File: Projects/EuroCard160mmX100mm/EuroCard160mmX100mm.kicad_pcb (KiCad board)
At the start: 2 copper layers, 159.8 x 99.8 mm, 0 parts

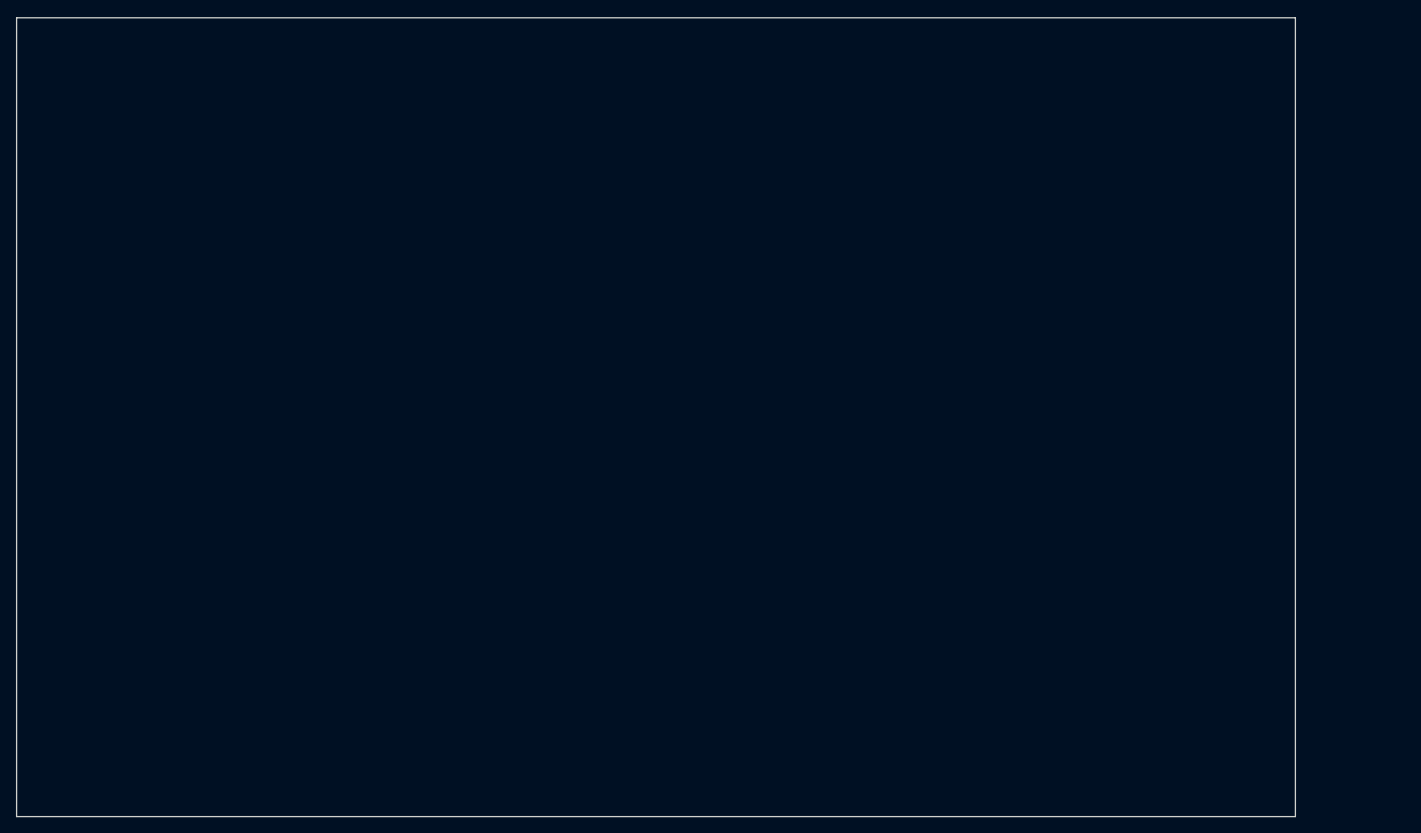
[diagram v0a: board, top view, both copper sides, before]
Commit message: Update EuroCard160mmX100mm* using KiCad 5.1.6
* Repointed all symbols and footprints to current libraries.
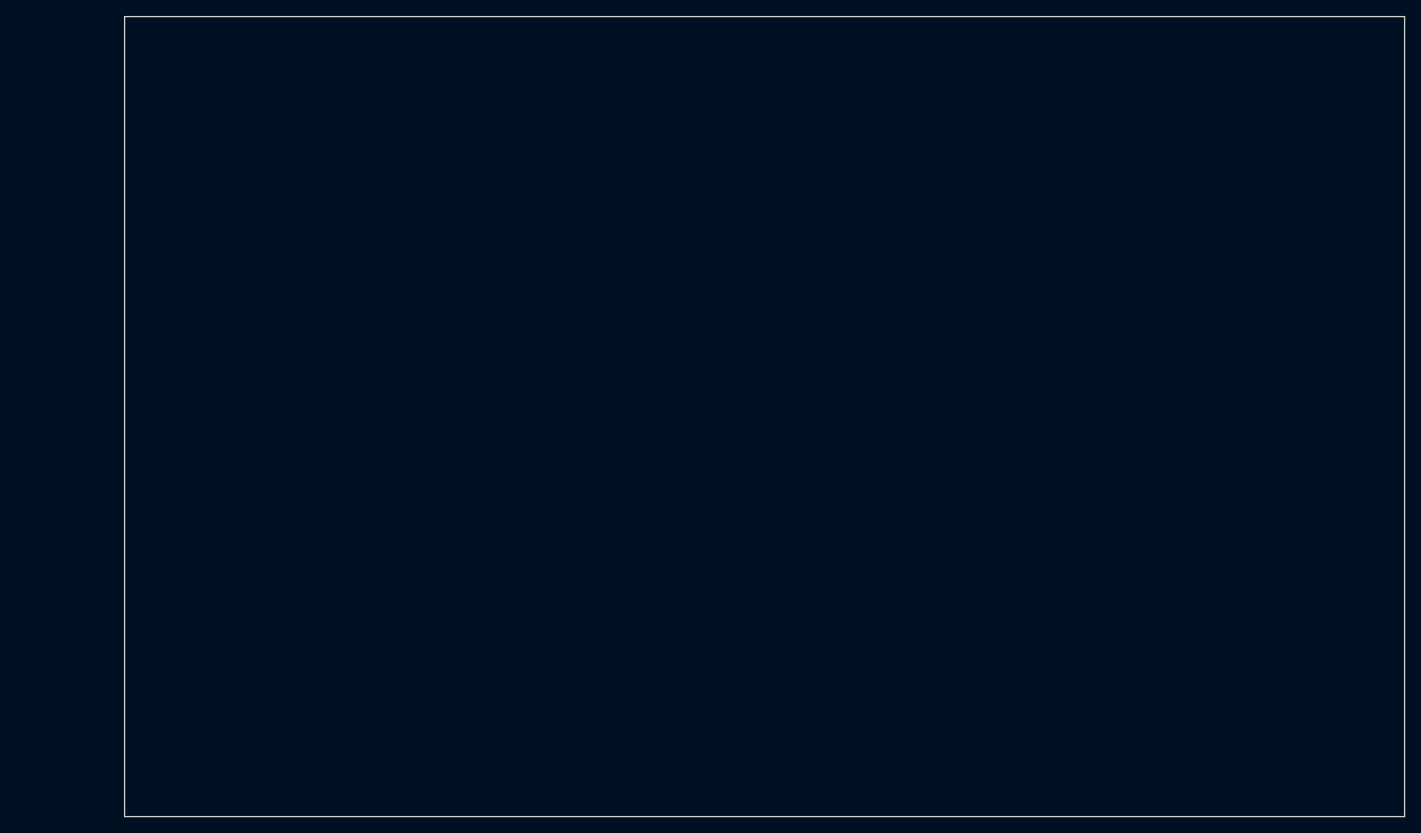
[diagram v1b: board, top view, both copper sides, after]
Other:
- board size 159.8 x 99.8 mm -> 160 x 100 mm
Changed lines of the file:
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@@
-(kicad_pcb (version 20170123) (host pcbnew "(2017-07-16 revision e797af331)-master")
+(kicad_pcb (version 20171130) (host pcbnew "(5.1.6)-1")
   (general
     (thickness 1.6)
@@
     (zone_45_only no)
     (trace_min 0.2)
-    (segment_width 0.2)
-    (edge_width 0.15)
     (via_size 0.8)
     (via_drill 0.4)
@@
     (uvia_min_size 0.2)
     (uvia_min_drill 0.1)
+    (edge_width 0.15)
+    (segment_width 0.2)
     (pcb_text_width 0.3)
     (pcb_text_size 1.5 1.5)
@@
     (pad_to_mask_clearance 0.2)
     (aux_axis_origin 0 0)
-    (grid_origin 55 145)
-    (visible_elements FFFFFF7F)
+    (grid_origin 68.5 45)
+    (visible_elements 7FFFFFFF)
     (pcbplotparams
       (layerselection 0x00030_ffffffff)
       (usegerberextensions false)
+      (usegerberattributes true)
+      (usegerberadvancedattributes true)
+      (creategerberjobfile true)
       (excludeedgelayer true)
       (linewidth 0.100000)
@@
       (hpglpennumber 1)
       (hpglpenspeed 20)
-      (hpglpendiameter 15)
+      (hpglpendiameter 15.000000)
       (psnegative false)
       (psa4output false)
@@
     (uvia_drill 0.1)
   )
-  (gr_line (start 55 145) (end 214.85 145) (angle 90) (layer Edge.Cuts) (width 0.15))
-  (gr_line (start 55 45.15) (end 55 145) (angle 90) (layer Edge.Cuts) (width 0.15))
-  (gr_line (start 214.84 45.15) (end 55 45.15) (angle 90) (layer Edge.Cuts) (width 0.15))
-  (gr_line (start 214.85 145) (end 214.85 45.15) (angle 90) (layer Edge.Cuts) (width 0.15))
+  (gr_line (start 68.5 145) (end 228.5 145) (angle 90) (layer Edge.Cuts) (width 0.15))
+  (gr_line (start 68.5 45) (end 68.5 145) (angle 90) (layer Edge.Cuts) (width 0.15))
+  (gr_line (start 228.5 45) (end 68.5 45) (angle 90) (layer Edge.Cuts) (width 0.15))
+  (gr_line (start 228.5 145) (end 228.5 45) (angle 90) (layer Edge.Cuts) (width 0.15))
 )
